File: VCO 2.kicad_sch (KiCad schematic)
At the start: 73 parts, among them J1 OUT 1x4s, J16 OCT_SW 1x7s, J18 CV 1x6s, J2 SIN 1x5s, J20 CTRL 1x9s, J85 Eurorack 2x8hs, J9 IN 1x6s, Q1 2N3904, Q2 2N3904, U1 CEM3340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

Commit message: Added +5v ref supply
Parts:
- added C12, C2: 0.1μF, Capacitor_THT:C_Disc_D4.7mm_W2.5mm_P5.00mm, symbol Device:C
- added R37: 4K7, Resistor_THT:R_Axial_DIN0204_L3.6mm_D1.6mm_P7.62mm_Horizontal, symbol Device:R
- added R38, R39: 33K, Resistor_THT:R_Axial_DIN0204_L3.6mm_D1.6mm_P7.62mm_Horizontal, symbol Device:R
- added R40: 10K, Resistor_THT:R_Axial_DIN0204_L3.6mm_D1.6mm_P7.62mm_Horizontal, symbol Device:R
- added R41: 9K, Resistor_THT:R_Axial_DIN0204_L3.6mm_D1.6mm_P7.62mm_Horizontal, symbol Device:R
- added R42: 530K, Resistor_THT:R_Axial_DIN0204_L3.6mm_D1.6mm_P7.62mm_Horizontal, symbol Device:R
- added U4: LM336Z-2.5/LFT3, Voltage Ref Diode:Z03A, symbol Voltage Ref Diode:LM336Z-2.5_LFT3
- R26: value 14K -> 4K7
- RV4: value REF 10K -> REF 1K
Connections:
- net +12V: now also R26.2; no longer R26.1
- net GND: now also C12.2, C2.2, R40.1, U4.3 (-V); no longer RV4.2, RV4.3, U3.12 (+)
- net at U3.13 (-), U3.14: now also R32.1
- net REF: now reaches J16.1 (Pin_1), R27.1, RV4.1, TP1.1
- net REF: now also RV4.2, U3.7; no longer R26.2
- net at U3.5 (+): now also R39.2; no longer J16.7 (Pin_7)
- new net: R40.2, R41.1, U3.6 (-)
- new net: C2.1, R38.2, R39.1
- new net: R37.1, R38.1, U4.2 (+V)
- new net: R42.2, RV4.3
- new net: R41.2, R42.1
- new net: J16.7 (Pin_7), U3.12 (+)
- new net: C12.1, R26.1, R37.2
- no-connect marks 6 -> 7
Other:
- note added: "+5V Ref voltage generator"
- note added: "CEM3340 and outputs"
- note added: "Octave selection and CV inputs"
- note added: "PWM, FM and Sync Inputs"
- note added: "Power input and smoothing"
- moved on the sheet: C1, H1, H2, H3, H4, J1, J16, J18, J2, Q1, Q2, R10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

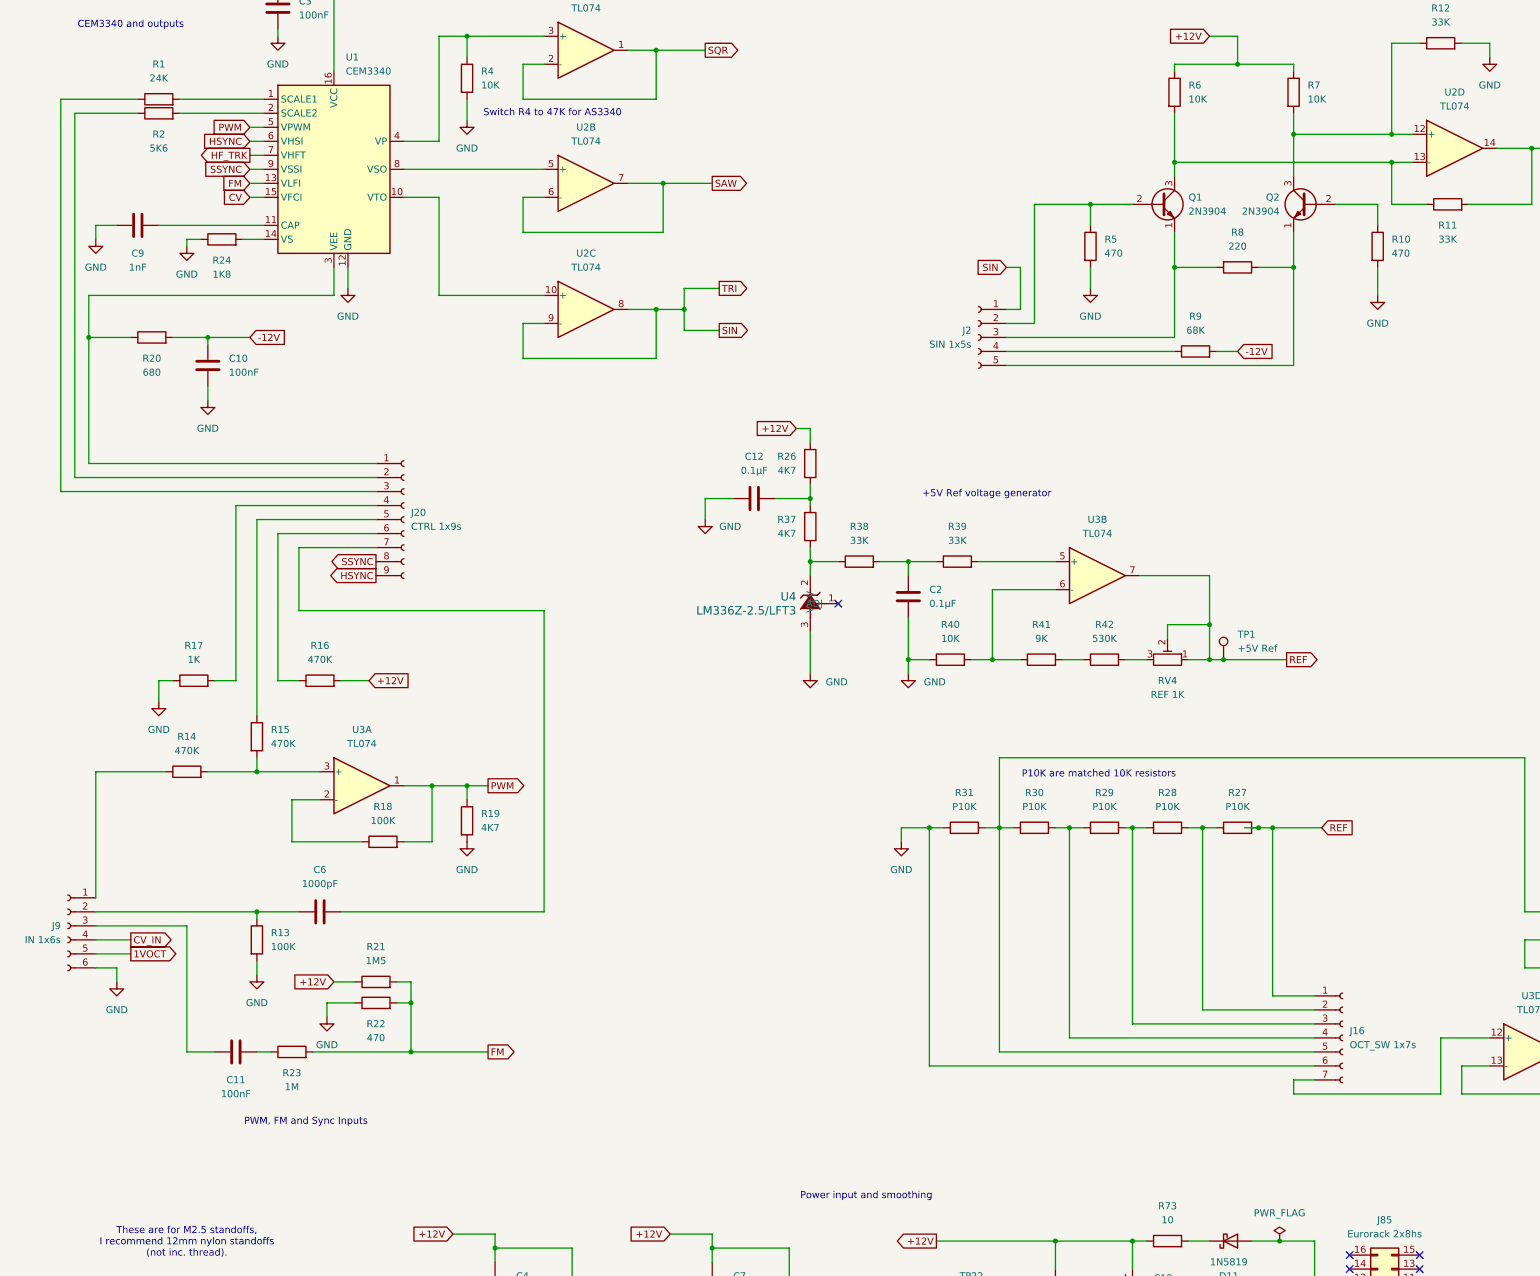
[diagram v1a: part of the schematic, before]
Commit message: +5V ref update
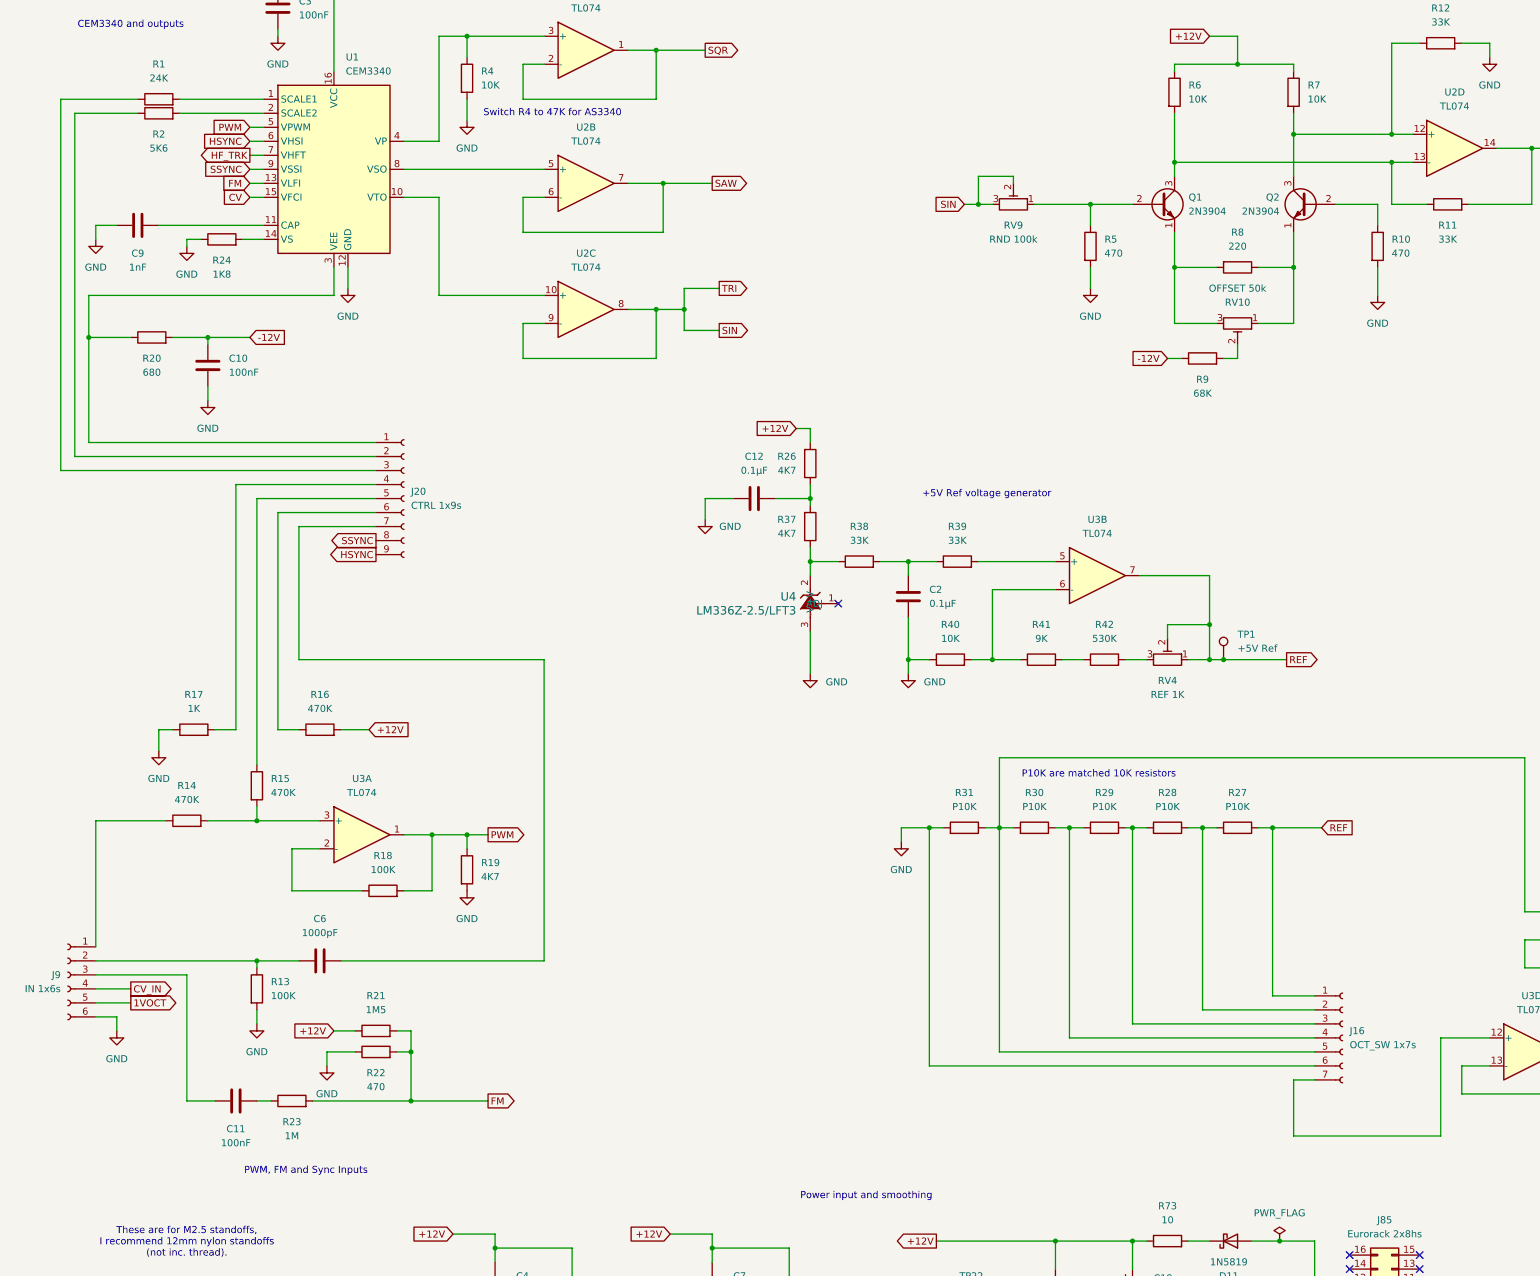
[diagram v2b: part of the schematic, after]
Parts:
- removed J2: SIN 1x5s, Connector_PinSocket_2.54mm:PinSocket_1x05_P2.54mm_Vertical, symbol Connector:Conn_01x05_Socket
- added RV10: OFFSET 50k, Potentiometer_THT:Potentiometer_Bourns_3296W_Vertical, symbol Device:R_Potentiometer_Trim
- added RV9: RND 100k, Potentiometer_THT:Potentiometer_Bourns_3296W_Vertical, symbol Device:R_Potentiometer_Trim
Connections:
- net -12V: now also R9.1; no longer R9.2
- net SIN: now also RV9.2, RV9.3
- net at Q1.2 (B), R5.1: now also RV9.1
- net at Q1.1 (E), R8.2: now also RV10.3
- net at Q2.1 (E), R8.1: now also RV10.1
- new net: R9.2, RV10.2
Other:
- moved on the sheet: C11, C6, J20, J9, R13, R14, R15, R16, R17, R18, R19, R21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

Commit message: Corrected output jack sockets
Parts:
- R42: value 530K -> 530
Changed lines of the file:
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@@
 			)
 		)
-		(property "Value" "530K"
+		(property "Value" "530"
 			(at 210.82 135.89 90)
 			(effects

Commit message: Updated ref design
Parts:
- C2: value 0.1μF -> 10μF
- R41: value 9K -> 9.1K
- R42: value 530 -> 510
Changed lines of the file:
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@@
 			)
 		)
-		(property "Value" "9K"
+		(property "Value" "9.1K"
 			(at 199.39 135.89 90)
 			(effects
@@
 			)
 		)
-		(property "Value" "530"
+		(property "Value" "510"
 			(at 210.82 135.89 90)
 			(effects
@@
 			)
 		)
-		(property "Value" "0.1μF"
+		(property "Value" "10μF"
 			(at 179.07 129.5399 0)
 			(effects

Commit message: Updates to jacks
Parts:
- added C13: 1nF, symbol Device:C
- R21: value 1M5 -> 1M2
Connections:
- net GND: now also C13.1; no longer R22.1
- new net: C13.2, R22.1
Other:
- note added: "VCO II (main board)"
- moved on the sheet: R21, R22
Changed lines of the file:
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@@
 		)
 	)
+	(text "VCO II (main board)"
+		(exclude_from_sim no)
+		(at 328.93 276.606 0)
+		(effects
+			(font
+				(size 2.54 2.54)
+			)
+		)
+	)
 	(text "Octave selection and CV inputs"
 		(exclude_from_sim no)
@@
 	)
 	(junction
+		(at 93.98 219.71)
+		(diameter 0)
+		(color 0 0 0 0)
+	)
+	(junction
 		(at 328.93 210.82)
 		(diameter 0)
@@
 	)
 	(junction
-		(at 85.09 219.71)
-		(diameter 0)
-		(color 0 0 0 0)
-	)
-	(junction
 		(at 229.87 139.7)
 		(diameter 0)
@@
 	)
 	(junction
-		(at 85.09 210.82)
+		(at 93.98 210.82)
 		(diameter 0)
 		(color 0 0 0 0)
@@
 	(wire
 		(pts
-			(xy 82.55 210.82) (xy 85.09 210.82)
+			(xy 91.44 210.82) (xy 93.98 210.82)
 		)
 		(stroke
@@
 	(wire
 		(pts
+			(xy 68.58 210.82) (xy 72.39 210.82)
+		)
+		(stroke
+			(width 0)
+			(type default)
+		)
+	)
+	(wire
+		(pts
 			(xy 39.37 152.4) (xy 39.37 156.21)
 		)
@@
 	(wire
 		(pts
-			(xy 71.12 207.01) (xy 74.93 207.01)
+			(xy 93.98 219.71) (xy 99.06 219.71)
+		)
+		(stroke
+			(width 0)
+			(type default)
+		)
+	)
+	(wire
+		(pts
+			(xy 80.01 204.47) (xy 83.82 204.47)
 		)
 		(stroke
@@
 	(wire
 		(pts
-			(xy 85.09 207.01) (xy 85.09 210.82)
+			(xy 93.98 204.47) (xy 93.98 210.82)
 		)
 		(stroke
@@
 	(wire
 		(pts
-			(xy 74.93 210.82) (xy 69.85 210.82)
-		)
-		(stroke
-			(width 0)
-			(type default)
-		)
-	)
-	(wire
-		(pts
 			(xy 114.3 274.32) (xy 100.33 274.32)
 		)
@@
 	(wire
 		(pts
-			(xy 85.09 210.82) (xy 85.09 219.71)
+			(xy 93.98 210.82) (xy 93.98 219.71)
 		)
 		(stroke
@@
 	(wire
 		(pts
-			(xy 69.85 210.82) (xy 69.85 213.36)
+			(xy 68.58 210.82) (xy 68.58 213.36)
 		)
 		(stroke
@@
 	(wire
 		(pts
-			(xy 85.09 207.01) (xy 82.55 207.01)
+			(xy 93.98 204.47) (xy 91.44 204.47)
 		)
 		(stroke
@@
 	(wire
 		(pts
-			(xy 85.09 219.71) (xy 99.06 219.71)
-		)
-		(stroke
-			(width 0)
-			(type default)
-		)
-	)
-	(wire
-		(pts
 			(xy 55.88 43.18) (xy 58.42 43.18)
 		)
@@
 	(wire
 		(pts
+			(xy 80.01 210.82) (xy 83.82 210.82)
+		)
+		(stroke
+			(width 0)
+			(type default)
+		)
+	)
+	(wire
+		(pts
 			(xy 157.48 134.62) (xy 157.48 142.24)
 		)
@@
 	(wire
 		(pts
-			(xy 67.31 219.71) (xy 85.09 219.71)
+			(xy 67.31 219.71) (xy 93.98 219.71)
 		)
 		(stroke
@@
 	(global_label "+12V"
 		(shape input)
-		(at 71.12 207.01 180)
+		(at 80.01 204.47 180)
 		(fields_autoplaced yes)
 		(effects
@@
 		)
 		(property "Intersheetrefs" "${INTERSHEET_REFS}"
-			(at 63.0548 207.01 0)
+			(at 71.9448 204.47 0)
 			(effects
 				(font
@@
 	(symbol
 		(lib_id "power:GND")
-		(at 69.85 213.36 0)
+		(at 68.58 213.36 0)
 		(unit 1)
 		(exclude_from_sim no)
@@
 		(fields_autoplaced yes)
 		(property "Reference" "#PWR028"
-			(at 69.85 219.71 0)
+			(at 68.58 219.71 0)
 			(effects
 				(font
@@
 		)
 		(property "Value" "GND"
-			(at 69.85 218.44 0)
+			(at 68.58 218.44 0)
 			(effects
 				(font
@@
 		)
 		(property "Footprint" ""
-			(at 69.85 213.36 0)
+			(at 68.58 213.36 0)
 			(effects
 				(font
@@
 		)
 		(property "Datasheet" ""
-			(at 69.85 213.36 0)
+			(at 68.58 213.36 0)
 			(effects
 				(font
@@
 		)
 		(property "Description" "Power symbol creates a global label with name \"GND\" , ground"
-			(at 69.85 213.36 0)
+			(at 68.58 213.36 0)
 			(effects
 				(font
@@
 	(symbol
 		(lib_id "Device:C")
+		(at 76.2 210.82 90)
+		(unit 1)
+		(exclude_from_sim no)
+		(in_bom yes)
+		(on_board yes)
+		(dnp no)
+		(fields_autoplaced yes)
+		(property "Reference" "C13"
+			(at 76.2 215.9 90)
+			(effects
+				(font
+					(size 1.27 1.27)
+				)
+			)
+		)
+		(property "Value" "1nF"
+			(at 76.2 218.44 90)
+			(effects
+				(font
+					(size 1.27 1.27)
+				)
+			)
+		)
+		(property "Footprint" ""
+			(at 80.01 209.8548 0)
+			(effects
+				(font
+					(size 1.27 1.27)
+				)
+				(hide yes)
+			)
+		)
+		(property "Datasheet" "~"
+			(at 76.2 210.82 0)
+			(effects
+				(font
+					(size 1.27 1.27)
+				)
+				(hide yes)
+			)
+		)
+		(property "Description" "Unpolarized capacitor"
+			(at 76.2 210.82 0)
+			(effects
+				(font
+					(size 1.27 1.27)
+				)
+				(hide yes)
+			)
+		)
+		(pin "1"
+		)
+		(pin "2"
+		)
+		(instances
+			(project ""
+				(path "/eb1652b6-57da-4a0e-88a4-449907a19840"
+					(reference "C13")
+					(unit 1)
+				)
+			)
+		)
+	)
+	(symbol
+		(lib_id "Device:C")
 		(at 139.7 267.97 0)
 		(unit 1)
@@
 	(symbol
 		(lib_id "Device:R")
-		(at 78.74 210.82 90)
+		(at 87.63 210.82 90)
 		(unit 1)
 		(exclude_from_sim no)
@@
 		(fields_autoplaced yes)
 		(property "Reference" "R22"
-			(at 78.74 214.63 90)
+			(at 87.63 214.63 90)
 			(effects
 				(font
@@
 		)
 		(property "Value" "470"
-			(at 78.74 217.17 90)
+			(at 87.63 217.17 90)
 			(effects
 				(font
@@
 		)
 		(property "Footprint" "Resistor_THT:R_Axial_DIN0204_L3.6mm_D1.6mm_P7.62mm_Horizontal"
-			(at 78.74 212.598 90)
+			(at 87.63 212.598 90)
 			(effects
 				(font
@@
 		)
 		(property "Datasheet" "~"
-			(at 78.74 210.82 0)
+			(at 87.63 210.82 0)
 			(effects
 				(font
@@
 		)
 		(property "Description" "Resistor"
-			(at 78.74 210.82 0)
+			(at 87.63 210.82 0)
 			(effects
 				(font
@@
 	(symbol
 		(lib_id "Device:R")
-		(at 78.74 207.01 90)
+		(at 87.63 204.47 90)
 		(unit 1)
 		(exclude_from_sim no)
@@
 		(fields_autoplaced yes)
 		(property "Reference" "R21"
-			(at 78.74 200.66 90)
+			(at 87.63 198.12 90)
 			(effects
 				(font
@@
 			)
 		)
-		(property "Value" "1M5"
-			(at 78.74 203.2 90)
+		(property "Value" "1M2"
+			(at 87.63 200.66 90)
 			(effects
 				(font
@@
 		)
 		(property "Footprint" "Resistor_THT:R_Axial_DIN0204_L3.6mm_D1.6mm_P7.62mm_Horizontal"
-			(at 78.74 208.788 90)
+			(at 87.63 206.248 90)
 			(effects
 				(font
@@
 		)
 		(property "Datasheet" "~"
-			(at 78.74 207.01 0)
+			(at 87.63 204.47 0)
 			(effects
 				(font
@@
 		)
 		(property "Description" "Resistor"
-			(at 78.74 207.01 0)
+			(at 87.63 204.47 0)
 			(effects
 				(font
